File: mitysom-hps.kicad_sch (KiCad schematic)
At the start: 7 parts, among them J100 Plug_Samtec_SEAM-50-02.0-L-08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

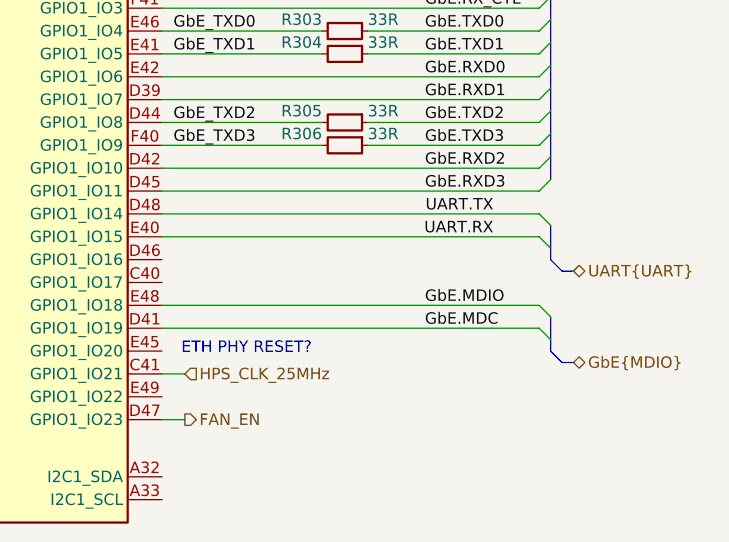
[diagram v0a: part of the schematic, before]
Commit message: [#100282] Connect I3C for CLK
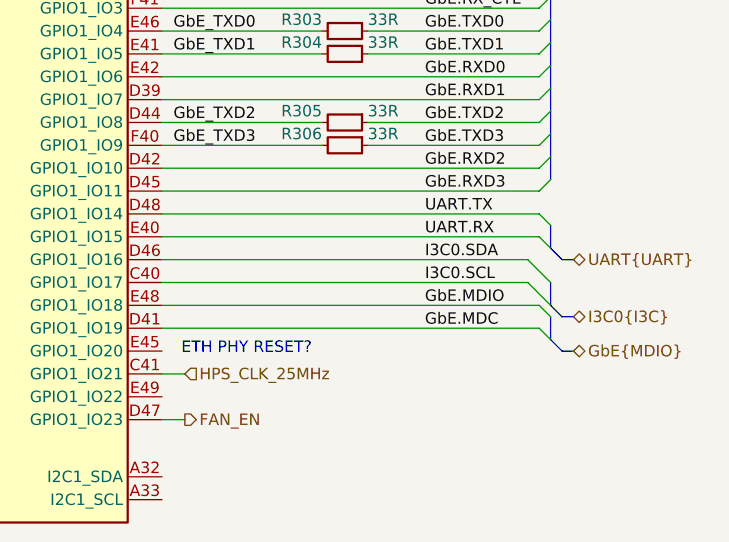
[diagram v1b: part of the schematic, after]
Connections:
- net I3C0.SCL: now reaches J100.C40 (GPIO1_IO17)
- net I3C0.SDA: now reaches J100.D46 (GPIO1_IO16)
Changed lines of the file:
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@@
+	)
+	(bus_entry
+		(at 262.89 163.83)
+		(size -2.54 -2.54)
+		(stroke
+			(width 0)
+			(type default)
+		)
 	)
 	(bus_entry
@@
 	)
 	(bus_entry
+		(at 262.89 166.37)
+		(size -2.54 -2.54)
+		(stroke
+			(width 0)
+			(type default)
+		)
+	)
+	(bus_entry
 		(at 262.89 132.08)
 		(size -1.27 1.27)
@@
 	(bus
 		(pts
-			(xy 265.43 172.72) (xy 264.16 172.72)
+			(xy 265.43 171.45) (xy 264.16 171.45)
 		)
 		(stroke
@@
 	(bus
 		(pts
-			(xy 264.16 162.56) (xy 265.43 162.56)
+			(xy 264.16 161.29) (xy 265.43 161.29)
 		)
 		(stroke
@@
 	(bus
 		(pts
-			(xy 264.16 162.56) (xy 262.89 161.29)
+			(xy 264.16 161.29) (xy 262.89 160.02)
 		)
 		(stroke
@@
 	(bus
 		(pts
-			(xy 264.16 172.72) (xy 262.89 171.45)
+			(xy 265.43 167.64) (xy 264.16 167.64)
+		)
+		(stroke
+			(width 0)
+			(type default)
+		)
+	)
+	(bus
+		(pts
+			(xy 264.16 171.45) (xy 262.89 170.18)
 		)
 		(stroke
@@
 		)
 	)
+	(bus
+		(pts
+			(xy 262.89 163.83) (xy 262.89 166.37)
+		)
+		(stroke
+			(width 0)
+			(type default)
+		)
+	)
+	(bus
+		(pts
+			(xy 264.16 167.64) (xy 262.89 166.37)
+		)
+		(stroke
+			(width 0)
+			(type default)
+		)
+	)
 	(wire
 		(pts
@@
 		)
 	)
+	(wire
+		(pts
+			(xy 219.71 163.83) (xy 260.35 163.83)
+		)
+		(stroke
+			(width 0)
+			(type default)
+		)
+	)
 	(bus
 		(pts
@@
 	(bus
 		(pts
-			(xy 262.89 161.29) (xy 262.89 157.48)
+			(xy 262.89 160.02) (xy 262.89 157.48)
 		)
 		(stroke
@@
 	(wire
 		(pts
+			(xy 219.71 161.29) (xy 260.35 161.29)
+		)
+		(stroke
+			(width 0)
+			(type default)
+		)
+	)
+	(wire
+		(pts
 			(xy 219.71 143.51) (xy 261.62 143.51)
 		)
@@
 	(bus
 		(pts
-			(xy 262.89 167.64) (xy 262.89 171.45)
+			(xy 262.89 167.64) (xy 262.89 170.18)
 		)
 		(stroke
@@
 	)
 	(label "UART.RX"
-		(at 256.54 158.75 180)
-		(effects
-			(font
-				(size 1.27 1.27)
-			)
-			(justify right bottom)
+		(at 248.92 158.75 0)
+		(effects
+			(font
+				(size 1.27 1.27)
+			)
+			(justify left bottom)
 		)
 	)
@@
 		)
 	)
+	(label "I3C0.SDA"
+		(at 248.92 161.29 0)
+		(effects
+			(font
+				(size 1.27 1.27)
+			)
+			(justify left bottom)
+		)
+	)
 	(label "ULPI.~{RST}"
 		(at 179.07 153.67 180)
@@
 		)
 	)
+	(label "I3C0.SCL"
+		(at 248.92 163.83 0)
+		(effects
+			(font
+				(size 1.27 1.27)
+			)
+			(justify left bottom)
+		)
+	)
 	(label "GbE.RXD2"
 		(at 248.92 151.13 0)
@@
 	)
 	(label "UART.TX"
-		(at 256.54 156.21 180)
-		(effects
-			(font
-				(size 1.27 1.27)
-			)
-			(justify right bottom)
+		(at 248.92 156.21 0)
+		(effects
+			(font
+				(size 1.27 1.27)
+			)
+			(justify left bottom)
 		)
 	)
@@
 	(hierarchical_label "UART{UART}"
 		(shape bidirectional)
-		(at 265.43 162.56 0)
+		(at 265.43 161.29 0)
 		(effects
 			(font
@@
 	(hierarchical_label "GbE{MDIO}"
 		(shape bidirectional)
-		(at 265.43 172.72 0)
-		(effects
-			(font
+		(at 265.43 171.45 0)
+		(effects
+			(font
+				(size 1.27 1.27)
+			)
+			(justify left)
+		)
+	)
+	(hierarchical_label "I3C0{I3C}"
+		(shape bidirectional)
+		(at 265.43 167.64 0)
+		(effects
+			(font

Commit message: [#100282] Connect QSPI_ISO_SW and MCU LEDs signals
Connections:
- net LED1: now reaches J100.D34 (GPIO0_IO9)
- net LED2: now reaches J100.D36 (GPIO0_IO10)
- net LED0: now reaches J100.F36 (GPIO0_IO8)
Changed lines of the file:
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@@
+	(wire
+		(pts
+			(xy 186.69 146.05) (xy 167.64 146.05)
+		)
+		(stroke
+			(width 0)
+			(type default)
+		)
+	)
 	(wire
 		(pts
@@
 	(wire
 		(pts
+			(xy 186.69 151.13) (xy 167.64 151.13)
+		)
+		(stroke
+			(width 0)
+			(type default)
+		)
+	)
+	(wire
+		(pts
 			(xy 242.57 148.59) (xy 261.62 148.59)
 		)
@@
 		(pts
 			(xy 265.43 167.64) (xy 264.16 167.64)
+		)
+		(stroke
+			(width 0)
+			(type default)
+		)
+	)
+	(wire
+		(pts
+			(xy 186.69 148.59) (xy 167.64 148.59)
 		)
 		(stroke
@@
 		)
 	)
+	(hierarchical_label "LED1"
+		(shape output)
+		(at 167.64 148.59 180)
+		(effects
+			(font
+				(size 1.27 1.27)
+			)
+			(justify right)
+		)
+	)
 	(hierarchical_label "CLK_25MHz"
 		(shape output)
@@
 		)
 	)
+	(hierarchical_label "LED2"
+		(shape output)
+		(at 167.64 151.13 180)
+		(effects
+			(font
+				(size 1.27 1.27)
+			)
+			(justify right)
+		)
+	)
 	(hierarchical_label "FAN_EN"
 		(shape output)
@@
 		(effects
 			(font
+				(size 1.27 1.27)
+			)
+			(justify right)
+		)
+	)
+	(hierarchical_label "LED0"
+		(shape output)
+		(at 167.64 146.05 180)
+		(effects
+			(font

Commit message: [#100282] WIP: Clear ERC
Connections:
- no-connect marks 0 -> 4
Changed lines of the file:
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@@
 		)
+	)
+	(no_connect
+		(at 219.71 176.53)
+	)
+	(no_connect
+		(at 219.71 185.42)
+	)
+	(no_connect
+		(at 186.69 153.67)
+	)
+	(no_connect
+		(at 219.71 187.96)
 	)
 	(bus_entry

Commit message: [#100282] Connect ETH PHY reset to SOM
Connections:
- net ~{GbE_RESET}: now reaches J100.E45 (GPIO1_IO20)
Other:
- note removed: "ETH PHY RESET?"
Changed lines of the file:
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@@
-		)
-	)
-	(text "ETH PHY RESET?"
-		(exclude_from_sim no)
-		(at 229.108 171.196 0)
-		(effects
-			(font
-				(size 1.27 1.27)
-			)
 		)
 	)
@@
 		(pts
 			(xy 265.43 167.64) (xy 264.16 167.64)
+		)
+		(stroke
+			(width 0)
+			(type default)
+		)
+	)
+	(wire
+		(pts
+			(xy 219.71 171.45) (xy 222.25 171.45)
 		)
 		(stroke
@@
 		)
 	)
+	(hierarchical_label "~{GbE_RESET}"
+		(shape output)
+		(at 222.25 171.45 0)
+		(effects
+			(font
+				(size 1.27 1.27)
+			)
+			(justify left)
+		)
+	)
